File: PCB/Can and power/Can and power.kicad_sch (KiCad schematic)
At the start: 41 parts, among them J1 TPS54232DR, J3 HDR_143_1, J4 HDR_143_2, J5 SKT_146, J6 HDR_175, J7 Car connector, U1 SN65HVD230

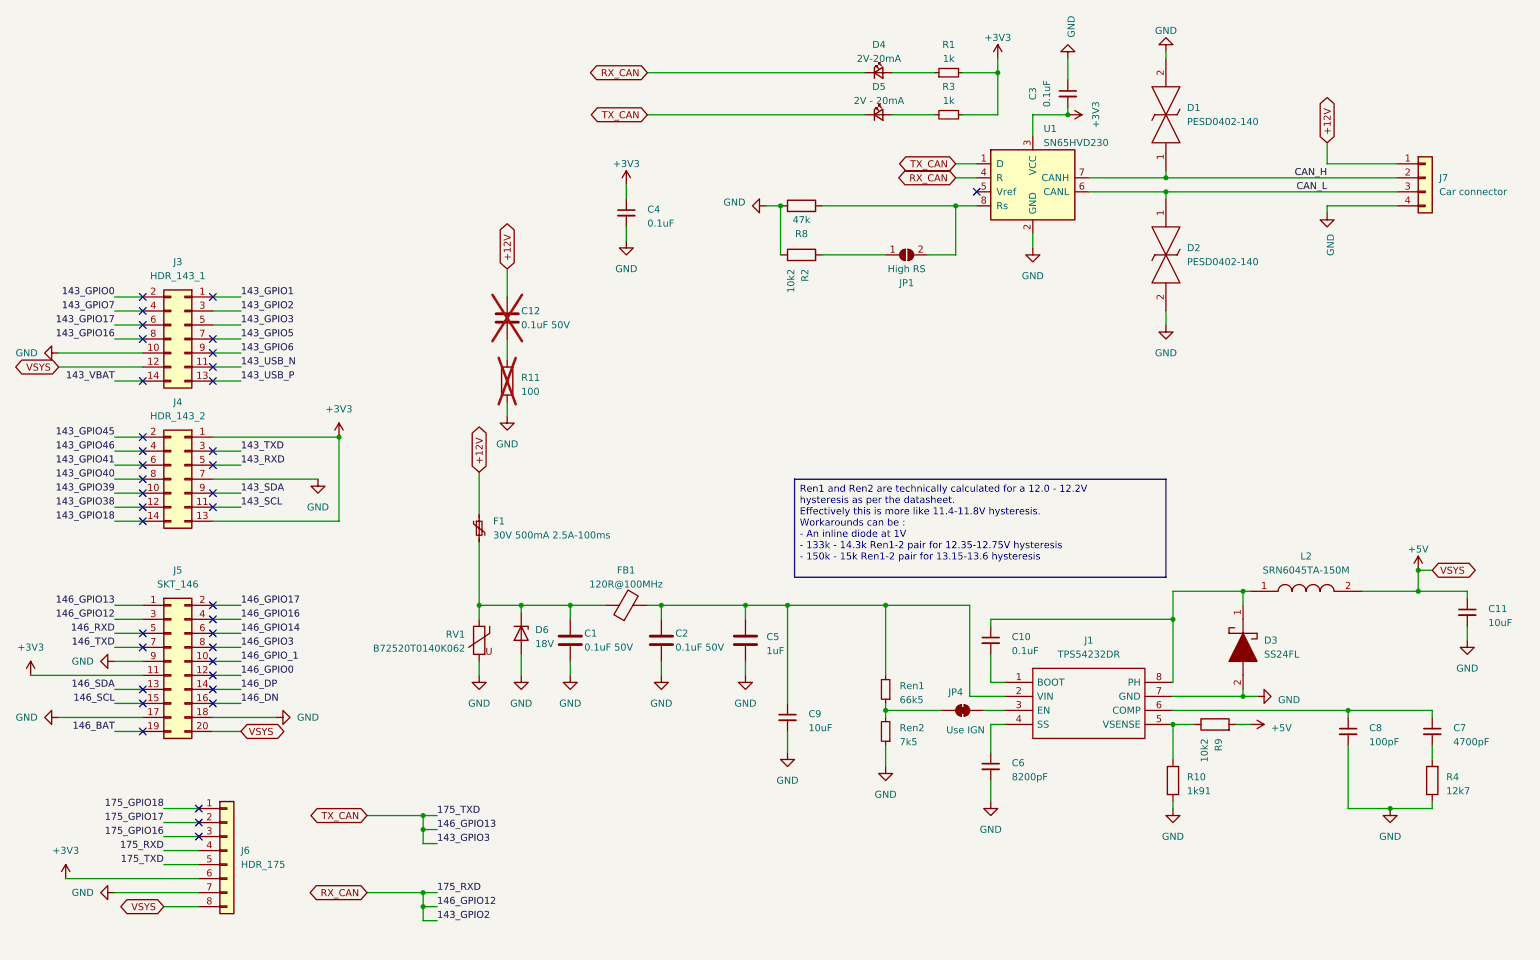
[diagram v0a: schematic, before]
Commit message: Digikey PN
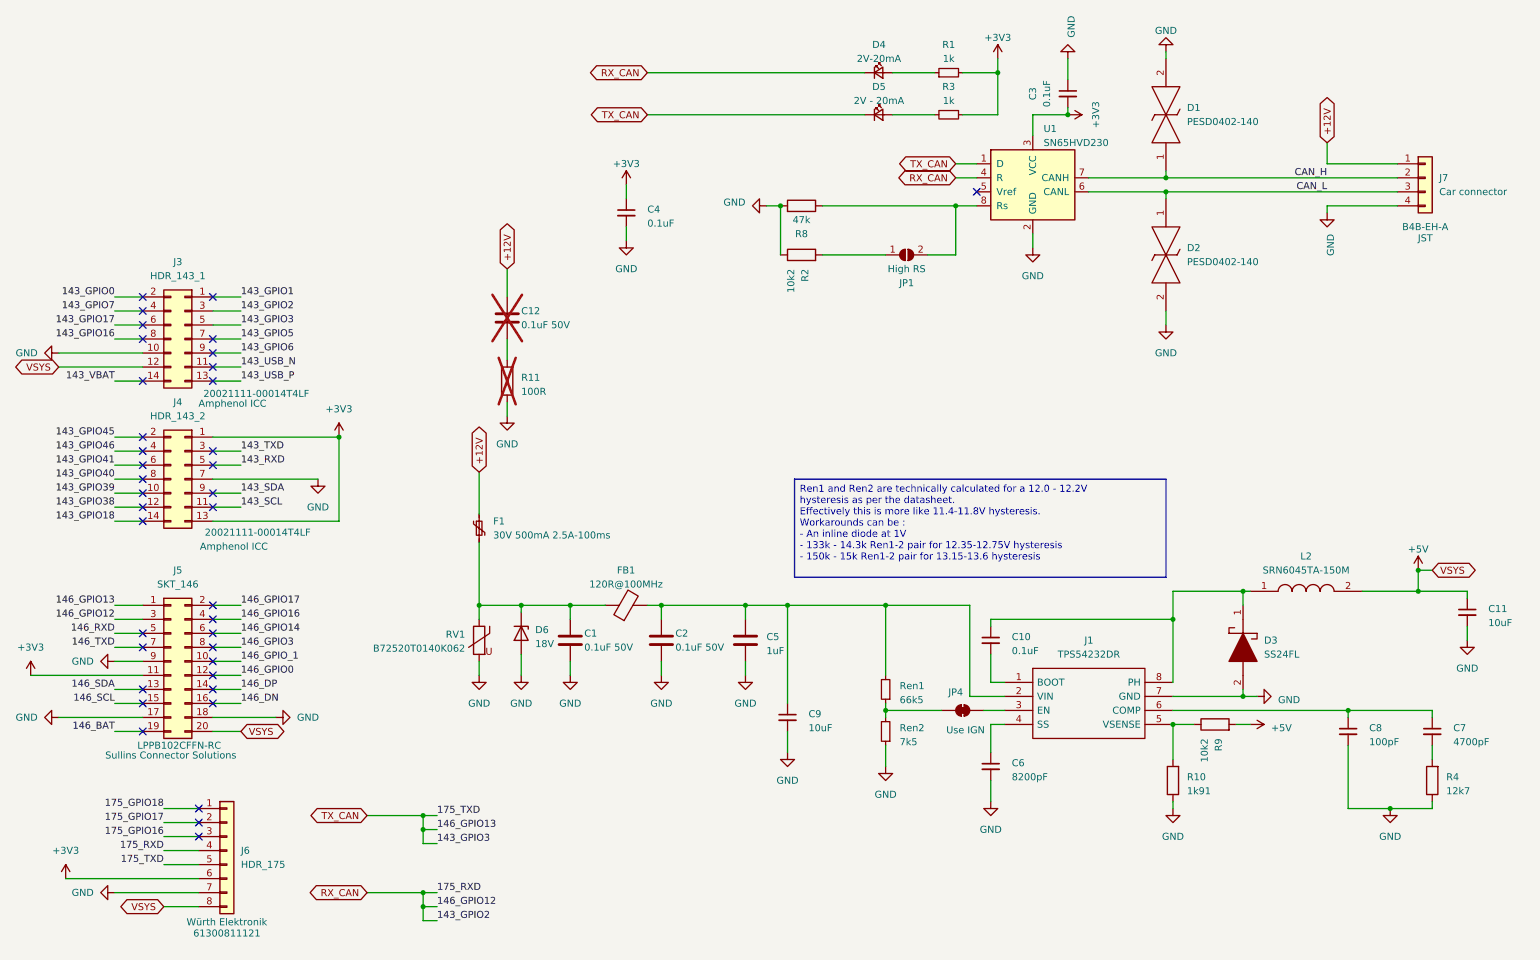
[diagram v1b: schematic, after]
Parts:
- C12: Manufacturer_Name (none) -> KEMET; Manufacturer_Part_Number (none) -> C1206C104K5RACTU
- J3, J4: Manufacturer_Name (none) -> Amphenol ICC; Manufacturer_Part_Number (none) -> 20021111-00014T4LF
- J5: Manufacturer_Name (none) -> Sullins Connector Solutions; Manufacturer_Part_Number (none) -> LPPB102CFFN-RC
- J6: Manufacturer_Name (none) -> Würth Elektronik; Manufacturer_Part_Number (none) -> 61300811121
- J7: Manufacturer_Name (none) -> JST; Manufacturer_Part_Number (none) -> B4B-EH-A
- R11: value 100 -> 100R; Manufacturer_Name (none) -> YAGEO; Manufacturer_Part_Number (none) -> RC1206FR-07100RL

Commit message: LCSC BOM finalisation
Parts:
- C1, C2: LCSC (none) -> C16194176; LCSC alt. (none) -> C16194176
- C10, C3, C4: LCSC (none) -> C108079; LCSC alt. (none) -> C108079
- C11: LCSC (none) -> C19702; LCSC alt. (none) -> C6119842
- C12: LCSC (none) -> C82601; LCSC alt. (none) -> C82601; Manufacturer_Name KEMET -> YAGEO; Manufacturer_Part_Number C1206C104K5RACTU -> CC1206KRX7R9BB104
- C5: LCSC (none) -> C92848; LCSC alt. (none) -> C15849
- C6: LCSC (none) -> C3883923; LCSC alt. (none) -> C1856442
- C7: LCSC (none) -> C3899730; LCSC alt. (none) -> C505480
- C8: LCSC (none) -> C20218600; LCSC alt. (none) -> C519407
- C9: LCSC (none) -> C14860; LCSC alt. (none) -> C14860
- D1, D2: LCSC (none) -> C10662; LCSC alt. (none) -> C19626256
- D3: LCSC (none) -> C894433; LCSC alt. (none) -> C894433
- D4: value 2V-20mA -> 2V - 20mA; LCSC (none) -> C157740; LCSC alt. (none) -> C157740; Manufacturer_Name Harvatek Corporation -> Lite-On; Manufacturer_Part_Number B1911UD--20D001014U1930 -> LTST-C190KFKT
- D5: LCSC (none) -> C157740; LCSC alt. (none) -> C157740; Manufacturer_Name Harvatek Corporation -> Lite-On; Manufacturer_Part_Number B1911UD--20D001014U1930 -> LTST-C190KFKT
- D6: LCSC (none) -> C668896; LCSC alt. (none) -> C467525
- F1: LCSC (none) -> C3760720; LCSC alt. (none) -> C720079; Manufacturer_Part_Number MF-USHT050KX-2 -> MF-USHT050KX
- FB1: LCSC alt. (none) -> C79382
- J1: LCSC (none) -> C52653; LCSC alt. (none) -> C52653
- J3, J4: LCSC (none) -> C5410334; LCSC alt. (none) -> C2935955
- J5: LCSC (none) -> C3319382; LCSC alt. (none) -> C22438134
- J6: LCSC (none) -> C492407; LCSC alt. (none) -> C492407
- J7: LCSC (none) -> C160258; LCSC alt. (none) -> C160258
- L2: LCSC (none) -> C1330797; LCSC alt. (none) -> C1330797
- R1, R3: LCSC (none) -> C22548; LCSC alt. (none) -> C22548
- R10: LCSC (none) -> C185353; LCSC alt. (none) -> C185353
- R11: LCSC (none) -> C137392; LCSC alt. (none) -> C17901
- R2, R9: LCSC (none) -> C183219; LCSC alt. (none) -> C183219
- R4: LCSC (none) -> C185374; LCSC alt. (none) -> C22866
- R8: LCSC (none) -> C278626; LCSC alt. (none) -> C105579
- RV1: LCSC alt. (none) -> C22355853
- Ren1: LCSC (none) -> C137691; LCSC alt. (none) -> C137691
- Ren2: LCSC (none) -> C114634; LCSC alt. (none) -> C114634
- U1: LCSC (none) -> C12084; LCSC alt. (none) -> C12084
